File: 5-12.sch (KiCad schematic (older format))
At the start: 9 parts, among them U1 ATmega32U4-AU

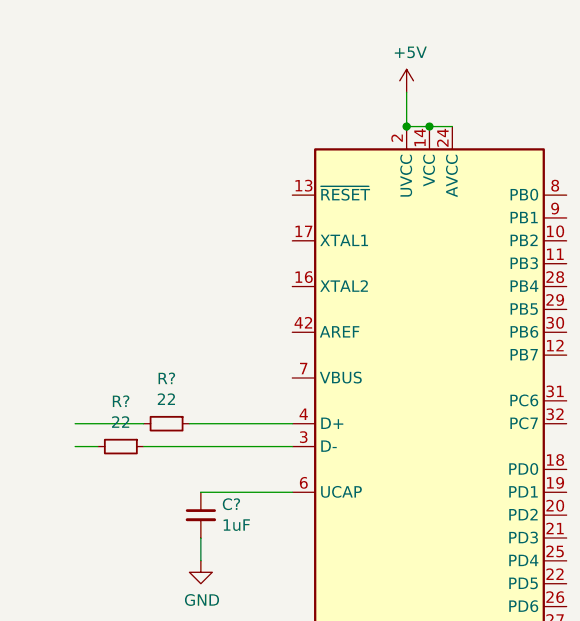
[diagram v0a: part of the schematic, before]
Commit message: Finishjed MCU zone on schematic
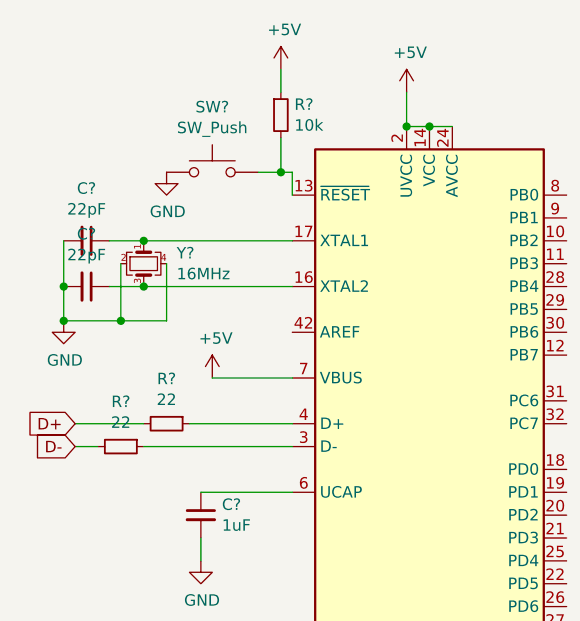
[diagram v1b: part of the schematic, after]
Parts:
- added C? (x2): 22pF, symbol Device:C_Small
- added R?: 10k, symbol Device:R_Small
- added SW?: SW_Push, symbol Switch:SW_Push
- added Y?: 16MHz, symbol Device:Crystal_GND24_Small
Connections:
- net labels added: D+, D-
- wire segments 19 -> 35
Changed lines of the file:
@@
 	1    0    0    -1
 $EndComp
+$Comp
+L power:+5V #PWR?
+U 1 1 5EBD4E68
+P 1550 2500
+F 0 "#PWR?" H 1550 2350 50  0001 C CNN
+F 1 "+5V" H 1565 2673 50  0000 C CNN
+F 2 "" H 1550 2500 50  0001 C CNN
+F 3 "" H 1550 2500 50  0001 C CNN
+	1    1550 2500
+	1    0    0    -1
+$EndComp
+Wire Wire Line
+	1550 2500 1900 2500
+$Comp
+L Device:Crystal_GND24_Small Y?
+U 1 1 5EBD658A
+P 1250 2000
+F 0 "Y?" V 1204 2144 50  0000 L CNN
+F 1 "16MHz" V 1295 2144 50  0000 L CNN
+F 2 "" H 1250 2000 50  0001 C CNN
+F 3 "~" H 1250 2000 50  0001 C CNN
+	1    1250 2000
+	0    1    1    0
+$EndComp
+Wire Wire Line
+	1250 1900 1900 1900
+Wire Wire Line
+	1900 2100 1250 2100
+$Comp
+L Device:C_Small C?
+U 1 1 5EBDA680
+P 1000 1900
+F 0 "C?" V 771 1900 50  0000 C CNN
+F 1 "22pF" V 862 1900 50  0000 C CNN
+F 2 "" H 1000 1900 50  0001 C CNN
+F 3 "~" H 1000 1900 50  0001 C CNN
+	1    1000 1900
+	0    1    1    0
+$EndComp
+$Comp
+L Device:C_Small C?
+U 1 1 5EBDB4B1
+P 1000 2100
+F 0 "C?" V 771 2100 50  0000 C CNN
+F 1 "22pF" V 862 2100 50  0000 C CNN
+F 2 "" H 1000 2100 50  0001 C CNN
+F 3 "~" H 1000 2100 50  0001 C CNN
+	1    1000 2100
+	0    1    1    0
+$EndComp
+$Comp
+L power:GND #PWR?
+U 1 1 5EBDB95F
+P 900 2250
+F 0 "#PWR?" H 900 2000 50  0001 C CNN
+F 1 "GND" H 905 2077 50  0000 C CNN
+F 2 "" H 900 2250 50  0001 C CNN
+F 3 "" H 900 2250 50  0001 C CNN
+	1    900  2250
+	1    0    0    -1
+$EndComp
+Wire Wire Line
+	900  2250 900  2100
+Connection ~ 900  2100
+Wire Wire Line
+	900  2100 900  1900
+Wire Wire Line
+	1100 1900 1250 1900
+Connection ~ 1250 1900
+Wire Wire Line
+	1100 2100 1250 2100
+Connection ~ 1250 2100
+Wire Wire Line
+	1150 2000 1150 2250
+Wire Wire Line
+	1350 2000 1350 2250
+Wire Wire Line
+	1350 2250 1150 2250
+Wire Wire Line
+	1150 2250 900  2250
+Connection ~ 1150 2250
+Connection ~ 900  2250
+$Comp
+L Switch:SW_Push SW?
+U 1 1 5EBDEC06
+P 1550 1600
+F 0 "SW?" H 1550 1885 50  0000 C CNN
+F 1 "SW_Push" H 1550 1794 50  0000 C CNN
+F 2 "" H 1550 1800 50  0001 C CNN
+F 3 "~" H 1550 1800 50  0001 C CNN
+	1    1550 1600
+	1    0    0    -1
+$EndComp
+$Comp
+L power:GND #PWR?
+U 1 1 5EBDFC51
+P 1350 1600
+F 0 "#PWR?" H 1350 1350 50  0001 C CNN
+F 1 "GND" H 1355 1427 50  0000 C CNN
+F 2 "" H 1350 1600 50  0001 C CNN
+F 3 "" H 1350 1600 50  0001 C CNN
+	1    1350 1600
+	1    0    0    -1
+$EndComp
+$Comp
+L Device:R_Small R?
+U 1 1 5EBE1E20
+P 1850 1350
+F 0 "R?" H 1909 1396 50  0000 L CNN
+F 1 "10k" H 1909 1305 50  0000 L CNN
+F 2 "" H 1850 1350 50  0001 C CNN
+F 3 "~" H 1850 1350 50  0001 C CNN
+	1    1850 1350
+	1    0    0    -1
+$EndComp
+$Comp
+L power:+5V #PWR?
+U 1 1 5EBE284C
+P 1850 1150
+F 0 "#PWR?" H 1850 1000 50  0001 C CNN
+F 1 "+5V" H 1865 1323 50  0000 C CNN
+F 2 "" H 1850 1150 50  0001 C CNN
+F 3 "" H 1850 1150 50  0001 C CNN
+	1    1850 1150
+	1    0    0    -1
+$EndComp
+Wire Wire Line
+	1850 1150 1850 1250
+Wire Wire Line
+	1900 1700 1900 1600
+Wire Wire Line
+	1900 1600 1850 1600
+Wire Wire Line
+	1850 1450 1850 1600
+Connection ~ 1850 1600
+Wire Wire Line
+	1850 1600 1750 1600
+Text GLabel 950  2700 0    50   Input ~ 0
+D+
+Text GLabel 950  2800 0    50   Input ~ 0
+D-
 $EndSCHEMATC

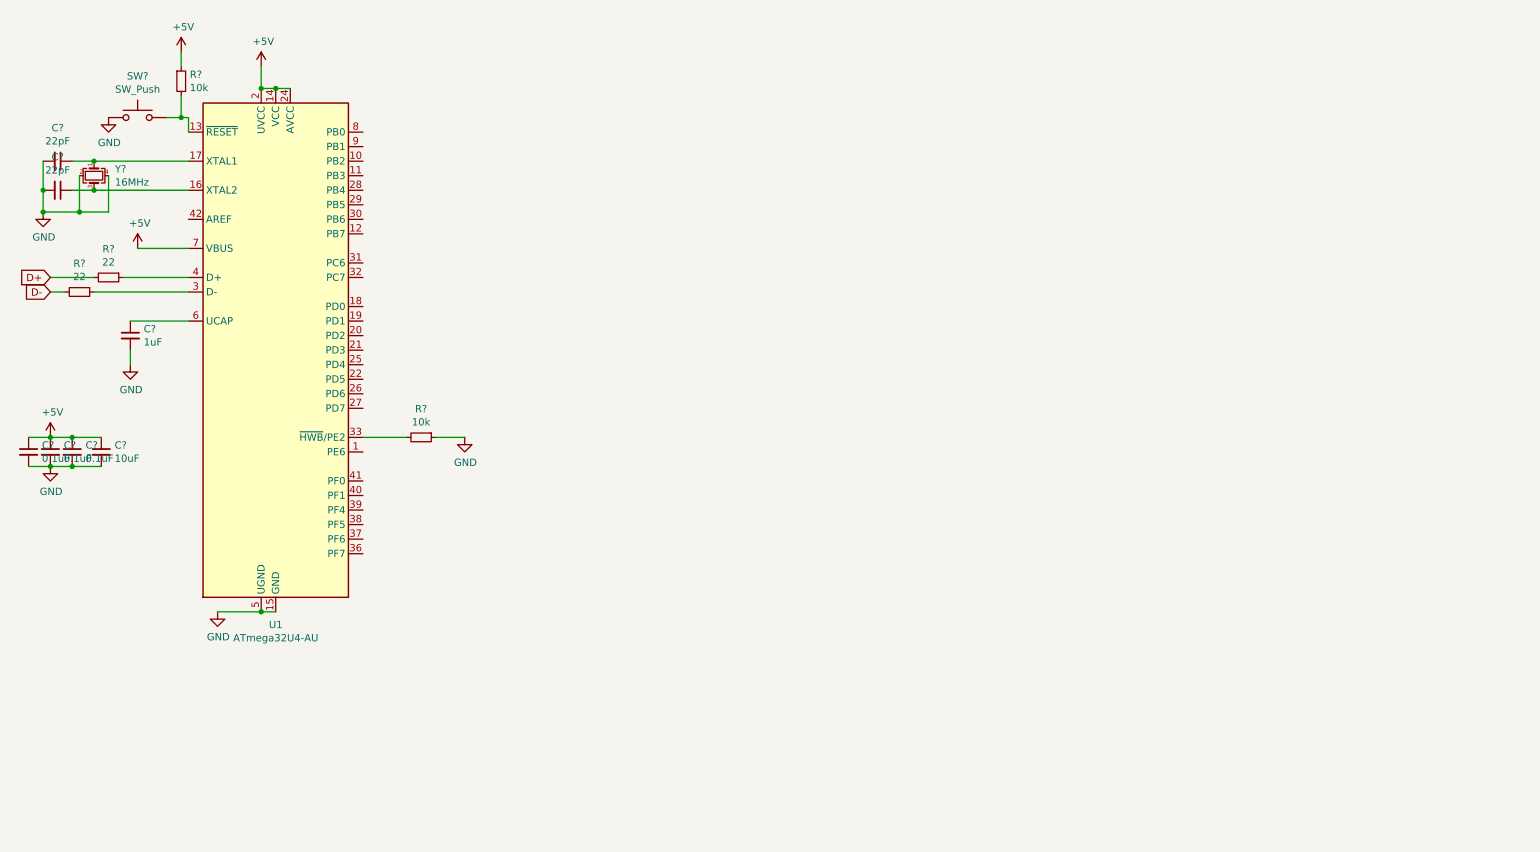
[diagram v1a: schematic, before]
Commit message: Added USB and uncpnnected switch matrix
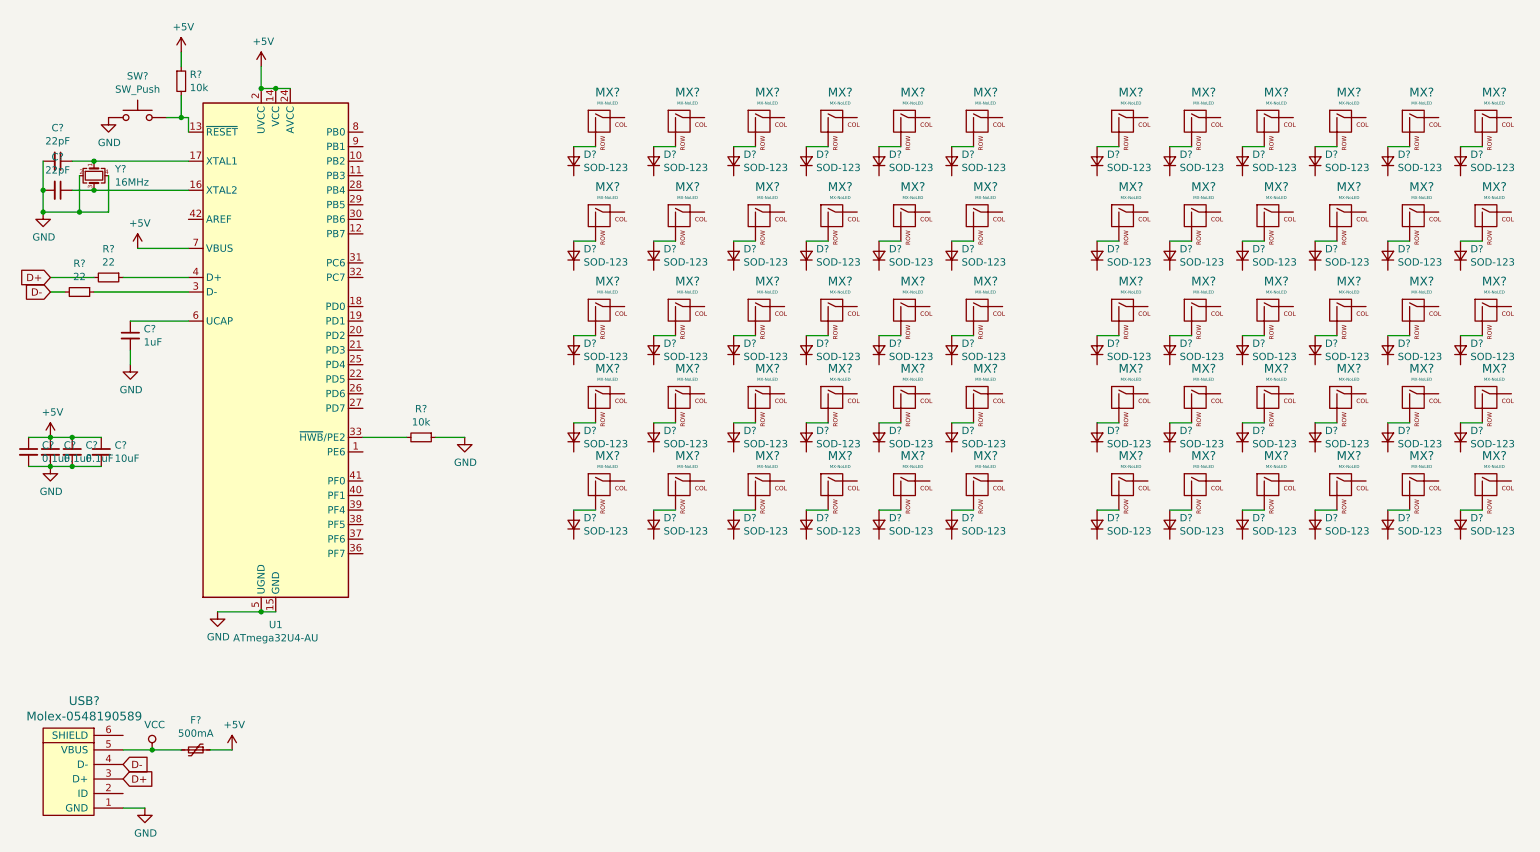
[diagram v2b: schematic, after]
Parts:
- added D? (x60): SOD-123, symbol Device:D_Small
- added F?: 500mA, symbol Device:Polyfuse_Small
- added MX? (x60): MX-NoLED, symbol MX_Alps_Hybrid:MX-NoLED
- added USB?: Molex-0548190589, symbol random-keyboard-parts:Molex-0548190589
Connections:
- net +5V: now also F?.1
- net D+: now also USB?.3 (D+)
- net D-: now also USB?.4 (D-)
- net GND: now also USB?.1 (GND)
- new net: D?.2 (A), MX?.2 (ROW) (x60)
- new net VCC: F?.2, USB?.5 (VBUS)

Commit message: added r, c tags for matrix
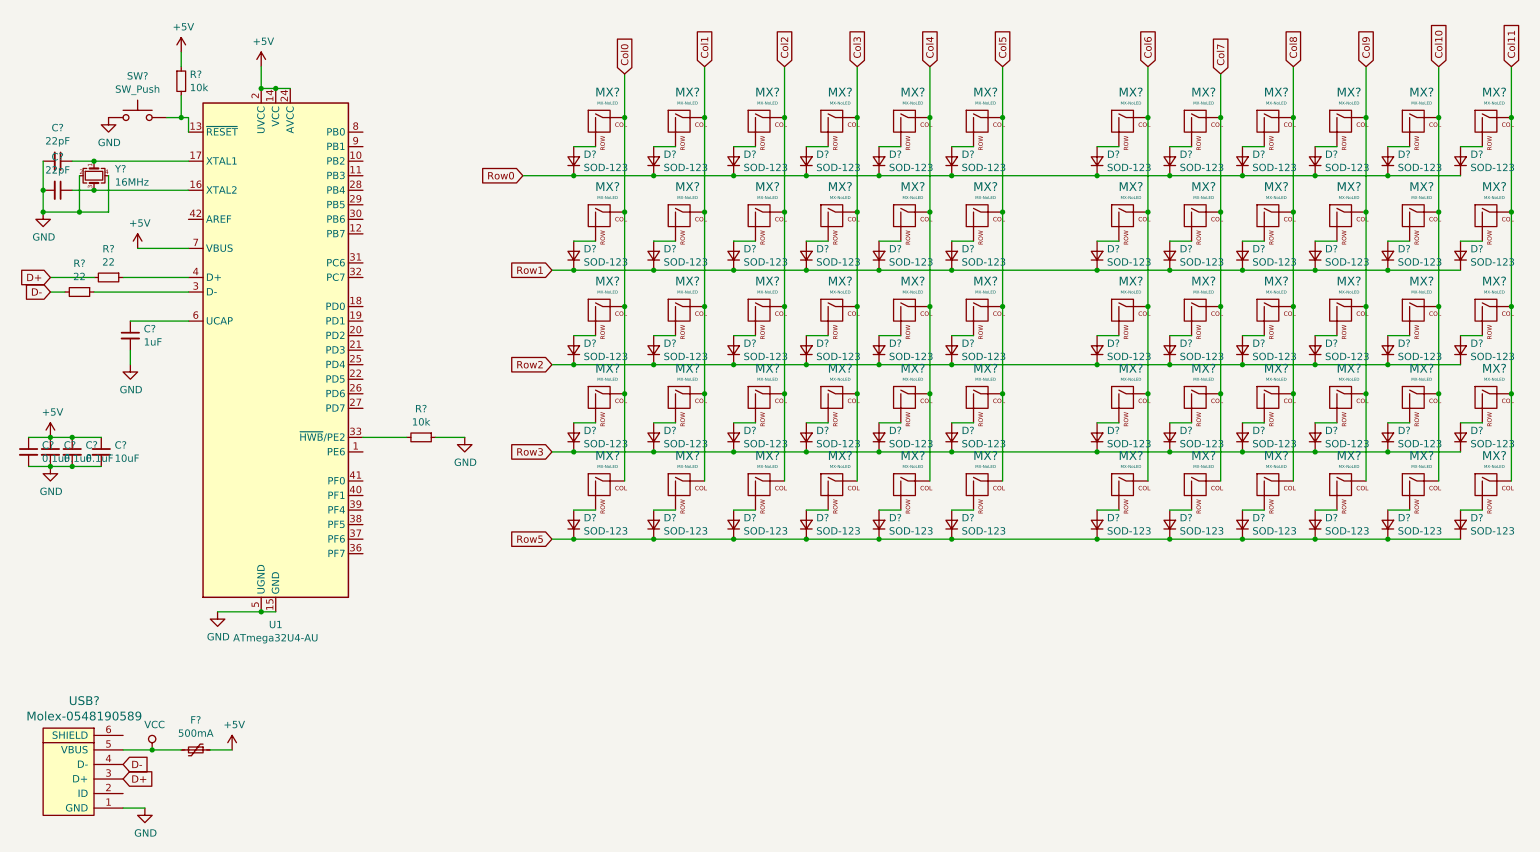
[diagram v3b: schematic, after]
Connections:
- net Col0: now reaches MX?.1 (COL)
- net Col0: now also MX?.1 (COL), MX?.1 (COL), MX?.1 (COL), MX?.1 (COL)
- net Row0: now reaches D?.1 (K)
- net Row0: now also D?.1 (K), D?.1 (K), D?.1 (K), D?.1 (K), D?.1 (K), D?.1 (K), D?.1 (K), D?.1 (K), D?.1 (K), D?.1 (K), D?.1 (K)
- net Row1: now reaches D?.1 (K)
- net Row1: now also D?.1 (K), D?.1 (K), D?.1 (K), D?.1 (K), D?.1 (K), D?.1 (K), D?.1 (K), D?.1 (K), D?.1 (K), D?.1 (K), D?.1 (K)
- net Row2: now reaches D?.1 (K)
- net Row2: now also D?.1 (K), D?.1 (K), D?.1 (K), D?.1 (K), D?.1 (K), D?.1 (K), D?.1 (K), D?.1 (K), D?.1 (K), D?.1 (K), D?.1 (K)
- net Row3: now reaches D?.1 (K)
- net Row3: now also D?.1 (K), D?.1 (K), D?.1 (K), D?.1 (K), D?.1 (K), D?.1 (K), D?.1 (K), D?.1 (K), D?.1 (K), D?.1 (K), D?.1 (K)
- net Row5: now reaches D?.1 (K)
- net Row5: now also D?.1 (K), D?.1 (K), D?.1 (K), D?.1 (K), D?.1 (K), D?.1 (K), D?.1 (K), D?.1 (K), D?.1 (K), D?.1 (K), D?.1 (K)
- net Col1: now reaches MX?.1 (COL)
- net Col1: now also MX?.1 (COL), MX?.1 (COL), MX?.1 (COL), MX?.1 (COL)
- net Col2: now reaches MX?.1 (COL)
- net Col2: now also MX?.1 (COL), MX?.1 (COL), MX?.1 (COL), MX?.1 (COL)
- net Col3: now reaches MX?.1 (COL)
- net Col3: now also MX?.1 (COL), MX?.1 (COL), MX?.1 (COL), MX?.1 (COL)
- net Col4: now reaches MX?.1 (COL)
- net Col4: now also MX?.1 (COL), MX?.1 (COL), MX?.1 (COL), MX?.1 (COL)
- net Col5: now reaches MX?.1 (COL)
- net Col5: now also MX?.1 (COL), MX?.1 (COL), MX?.1 (COL), MX?.1 (COL)
- net Col6: now reaches MX?.1 (COL)
- net Col6: now also MX?.1 (COL), MX?.1 (COL), MX?.1 (COL), MX?.1 (COL)
- net Col7: now reaches MX?.1 (COL)
- net Col7: now also MX?.1 (COL), MX?.1 (COL), MX?.1 (COL), MX?.1 (COL)
- net Col8: now reaches MX?.1 (COL)
- net Col8: now also MX?.1 (COL), MX?.1 (COL), MX?.1 (COL), MX?.1 (COL)
- net Col9: now reaches MX?.1 (COL)
- net Col9: now also MX?.1 (COL), MX?.1 (COL), MX?.1 (COL), MX?.1 (COL)
- net Col10: now reaches MX?.1 (COL)
- net Col10: now also MX?.1 (COL), MX?.1 (COL), MX?.1 (COL), MX?.1 (COL)
- net Col11: now reaches MX?.1 (COL)
- net Col11: now also MX?.1 (COL), MX?.1 (COL), MX?.1 (COL), MX?.1 (COL)
